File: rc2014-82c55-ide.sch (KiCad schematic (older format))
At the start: 13 parts, among them J1 CONN_02X06, J2 IDE connector, P1 RC2014 BUS, U1 82C55A_PLCC, U2 74HCT688, U3 74HCT04

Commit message: WIP
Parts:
- removed R2: 10K, Resistors_THT:R_Axial_DIN0207_L6.3mm_D2.5mm_P7.62mm_Horizontal, symbol R
- added J3: IDE connector, Pin_Headers:Pin_Header_Straight_2x22_Pitch2.00mm, symbol CONN_02X22
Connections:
- net labels added: RESET
- net labels removed: /INT0
- wire segments 166 -> 209
- no-connect marks 24 -> 30
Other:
- moved on the sheet: D1, J2, R1, U3B

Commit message: Relayout
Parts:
- removed J1: CONN_02X06, Pin_Headers:Pin_Header_Straight_2x06_Pitch2.54mm, symbol CONN_02X06
- added J1: CONN_02X13, Pin_Headers:Pin_Header_Straight_2x13_Pitch2.54mm, symbol CONN_02X13
- added SW1: SW_DIP_x06, Buttons_Switches_THT:SW_DIP_x6_W7.62mm_Slide, symbol SW_DIP_x06
- C1, C2, C3: footprint Capacitors_THT:C_Disc_D3.8mm_W2.6mm_P2.50mm -> Capacitors_THT:C_Disc_D3.0mm_W2.0mm_P2.50mm
- J2: footprint Pin_Headers:Pin_Header_Angled_2x20_Pitch2.54mm -> Pin_Headers:Pin_Header_Straight_2x20_Pitch2.54mm
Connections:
- net labels added: PC2, PC4, PC6
- net labels removed: INTRQ
- wire segments 209 -> 240
- no-connect marks 30 -> 32
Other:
- note removed: "TODO: INTRQ from drive?\n\nWiring this to the Z80s interrupt pin will cause issues when operating the Z80 in interrupt Mode 2. \nHave left it disconnected for the time being."
- moved on the sheet: J3, U3A, U3C, U3D, U3E, U3F

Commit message: WIP
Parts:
- removed J1: CONN_02X13, Pin_Headers:Pin_Header_Straight_2x13_Pitch2.54mm, symbol CONN_02X13
- added J1: CONN_01X02, Connectors:PINHEAD1-2, symbol CONN_01X02
- added J5: CONN_01X03, Pin_Headers:Pin_Header_Straight_1x03_Pitch2.54mm, symbol CONN_01X03
- D1: footprint LEDs:LED_D3.0mm_Horizontal_O3.81mm_Z6.0mm -> LEDs:LED_D1.8mm_W3.3mm_H2.4mm
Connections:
- net labels added: EXT_VCC, IDE_VCC
- wire segments 240 -> 219
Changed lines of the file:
@@
 F 0 "D1" H 6150 2300 50  0000 C CNN
 F 1 "LED" H 6150 2100 50  0000 C CNN
-F 2 "LEDs:LED_D3.0mm_Horizontal_O3.81mm_Z6.0mm" H 6150 2200 50  0001 C CNN
+F 2 "LEDs:LED_D1.8mm_W3.3mm_H2.4mm" H 6150 2200 50  0001 C CNN
 F 3 "" H 6150 2200 50  0001 C CNN
 	1    6150 2200
@@
 Text Label 10450 3600 0    60   ~ 0
 IDE-GND
-$Comp
-L VCC #PWR012
-U 1 1 59B846DB
-P 10850 3500
-F 0 "#PWR012" H 10850 3350 50  0001 C CNN
-F 1 "VCC" H 10850 3650 50  0000 C CNN
-F 2 "" H 10850 3500 50  0001 C CNN
-F 3 "" H 10850 3500 50  0001 C CNN
-	1    10850 3500
-	0    1    1    0
-$EndComp
-$Comp
-L VCC #PWR013
-U 1 1 59B84713
-P 9350 3500
-F 0 "#PWR013" H 9350 3350 50  0001 C CNN
-F 1 "VCC" H 9350 3650 50  0000 C CNN
-F 2 "" H 9350 3500 50  0001 C CNN
-F 3 "" H 9350 3500 50  0001 C CNN
-	1    9350 3500
-	0    -1   -1   0
-$EndComp
 NoConn ~ 9350 3000
 NoConn ~ 7650 3000
@@
 Wire Wire Line
 	6500 5650 7000 5650
-$Comp
-L CONN_02X13 J1
-U 1 1 59C02D49
-P 2950 4650
-F 0 "J1" H 2950 5350 50  0000 C CNN
-F 1 "CONN_02X13" V 2950 4650 50  0000 C CNN
-F 2 "Pin_Headers:Pin_Header_Straight_2x13_Pitch2.54mm" H 2950 3500 50  0001 C CNN
-F 3 "" H 2950 3500 50  0001 C CNN
-	1    2950 4650
-	1    0    0    -1
-$EndComp
-Wire Wire Line
-	2700 4050 2350 4050
-Wire Wire Line
-	2700 4150 2350 4150
-Wire Wire Line
-	2700 4250 2350 4250
-Wire Wire Line
-	2700 4350 2350 4350
-Wire Wire Line
-	2700 4450 2350 4450
-Wire Wire Line
-	2700 4550 2350 4550
-Wire Wire Line
-	2700 4650 2350 4650
-Wire Wire Line
-	2700 4750 2350 4750
-Wire Wire Line
-	2700 4850 2350 4850
-Wire Wire Line
-	2700 4950 2350 4950
-Wire Wire Line
-	2700 5050 2350 5050
-Wire Wire Line
-	2700 5150 2350 5150
-Wire Wire Line
-	2700 5250 2350 5250
-Wire Wire Line
-	3550 4050 3200 4050
-Wire Wire Line
-	3200 4150 3550 4150
-Wire Wire Line
-	3200 4250 3550 4250
-Wire Wire Line
-	3200 4350 3550 4350
-Wire Wire Line
-	3200 4450 3550 4450
-Wire Wire Line
-	3200 4550 3550 4550
-Wire Wire Line
-	3200 4650 3550 4650
-Wire Wire Line
-	3200 4750 3550 4750
-Wire Wire Line
-	3200 4850 3550 4850
-Wire Wire Line
-	3200 4950 3550 4950
-Wire Wire Line
-	3200 5050 3550 5050
-Wire Wire Line
-	3200 5150 3550 5150
-Wire Wire Line
-	3200 5250 3550 5250
-Text Label 2400 4050 0    60   ~ 0
-PC0
-Text Label 2400 4150 0    60   ~ 0
-PC1
-Text Label 2400 4250 0    60   ~ 0
-PC2
-Text Label 2400 4350 0    60   ~ 0
-PC3
-Text Label 2400 4450 0    60   ~ 0
-PC4
-Text Label 2400 4550 0    60   ~ 0
-PC5
-Text Label 2400 4650 0    60   ~ 0
-PC6
-Text Label 2400 4750 0    60   ~ 0
-PC7
-Text Label 2400 4850 0    60   ~ 0
-PB7
-Text Label 2400 4950 0    60   ~ 0
-PB6
-Text Label 2400 5050 0    60   ~ 0
-PB5
-Text Label 2400 5150 0    60   ~ 0
-PB4
-Text Label 3350 4050 0    60   ~ 0
-PA0
-Text Label 3350 4150 0    60   ~ 0
-PA1
-Text Label 3350 4250 0    60   ~ 0
-PA2
-Text Label 3350 4350 0    60   ~ 0
-PA3
-Text Label 3350 4450 0    60   ~ 0
-PA4
-Text Label 3350 4550 0    60   ~ 0
-PA5
-Text Label 3350 4650 0    60   ~ 0
-PA6
-Text Label 3350 4750 0    60   ~ 0
-PA7
-Text Label 3350 4850 0    60   ~ 0
-PB0
-Text Label 3350 4950 0    60   ~ 0
-PB1
-Text Label 3350 5050 0    60   ~ 0
-PB2
-Text Label 3350 5150 0    60   ~ 0
-PB3
-$Comp
-L GND #PWR014
-U 1 1 59C031E2
-P 3550 5250
-F 0 "#PWR014" H 3550 5000 50  0001 C CNN
-F 1 "GND" H 3550 5100 50  0000 C CNN
-F 2 "" H 3550 5250 50  0001 C CNN
-F 3 "" H 3550 5250 50  0001 C CNN
-	1    3550 5250
-	1    0    0    -1
-$EndComp
 Text Label 9150 6250 0    60   ~ 0
 PC7
@@
 PC3
 $Comp
-L VCC #PWR015
-U 1 1 59C0A089
-P 2350 5250
-F 0 "#PWR015" H 2350 5100 50  0001 C CNN
-F 1 "VCC" H 2350 5400 50  0000 C CNN
-F 2 "" H 2350 5250 50  0001 C CNN
-F 3 "" H 2350 5250 50  0001 C CNN
-	1    2350 5250
-	0    -1   -1   0
-$EndComp
-$Comp
 L SW_DIP_x06 SW1
 U 1 1 59C0ABDD
@@
 Text Label 7100 5150 0    60   ~ 0
 DA2
+$Comp
+L CONN_01X03 J5
+U 1 1 59C1C7A5
+P 8250 5000
+F 0 "J5" H 8250 5200 50  0000 C CNN
+F 1 "CONN_01X03" V 8350 5000 50  0000 C CNN
+F 2 "Pin_Headers:Pin_Header_Straight_1x03_Pitch2.54mm" H 8250 5000 50  0001 C CNN
+F 3 "" H 8250 5000 50  0001 C CNN
+	1    8250 5000
+	1    0    0    -1
+$EndComp
+Wire Wire Line
+	8050 4900 7800 4900
+Wire Wire Line
+	8050 5000 7800 5000
+Wire Wire Line
+	8050 5100 7800 5100
+Text Label 7800 5000 0    60   ~ 0
+IDE_VCC
+Text Label 7800 5100 0    60   ~ 0
+EXT_VCC
+$Comp
+L VCC #PWR012
+U 1 1 59C1C979
+P 7800 4900
+F 0 "#PWR012" H 7800 4750 50  0001 C CNN
+F 1 "VCC" H 7800 5050 50  0000 C CNN
+F 2 "" H 7800 4900 50  0001 C CNN
+F 3 "" H 7800 4900 50  0001 C CNN
+	1    7800 4900
+	0    -1   -1   0
+$EndComp
+$Comp
+L CONN_01X02 J1
+U 1 1 59C1C9D2
+P 8200 6000
+F 0 "J1" H 8200 6150 50  0000 C CNN
+F 1 "CONN_01X02" V 8300 6000 50  0000 C CNN
+F 2 "Connectors:PINHEAD1-2" H 8200 6000 50  0001 C CNN
+F 3 "" H 8200 6000 50  0001 C CNN
+	1    8200 6000
+	1    0    0    -1
+$EndComp
+Wire Wire Line
+	8000 5950 7750 5950
+Wire Wire Line
+	8000 6050 7750 6050
+Text Label 7750 5950 0    60   ~ 0
+EXT_VCC
+Text Label 9350 3500 0    60   ~ 0
+IDE_VCC
+Text Label 10500 3500 0    60   ~ 0
+IDE_VCC
+$Comp
+L GND #PWR013
+U 1 1 59C1D145
+P 7750 6050
+F 0 "#PWR013" H 7750 5800 50  0001 C CNN
+F 1 "GND" H 7750 5900 50  0000 C CNN
+F 2 "" H 7750 6050 50  0001 C CNN
+F 3 "" H 7750 6050 50  0001 C CNN
+	1    7750 6050
+	1    0    0    -1
+$EndComp
 $EndSCHEMATC

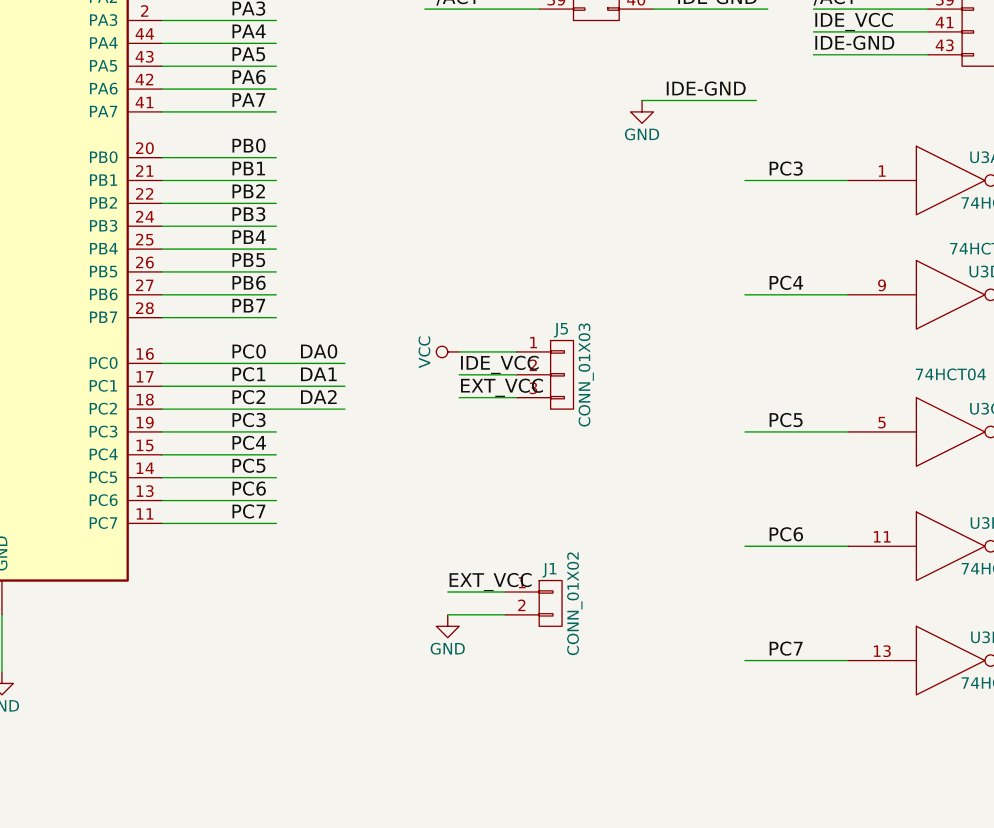
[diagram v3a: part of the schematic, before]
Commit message: Add jumpers
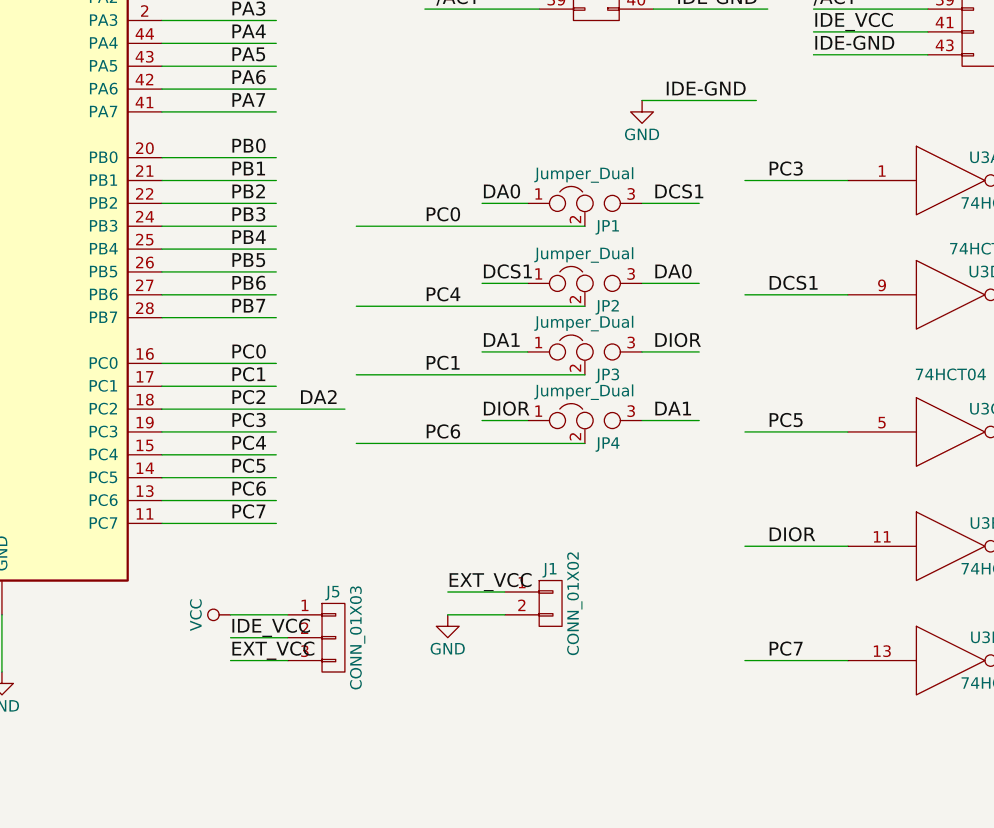
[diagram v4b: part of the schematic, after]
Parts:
- added JP1, JP2, JP3, JP4: Jumper_Dual, symbol Jumper_Dual
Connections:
- net labels added: DCS1, DIOR
- wire segments 219 -> 232
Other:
- moved on the sheet: J5
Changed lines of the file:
@@
 5V
 $Comp
-L VCC #PWR01
+L VCC #PWR2
 U 1 1 5898D2A5
 P 1350 3500
-F 0 "#PWR01" H 1350 3350 50  0001 C CNN
+F 0 "#PWR2" H 1350 3350 50  0001 C CNN
 F 1 "VCC" H 1600 3500 50  0000 C CNN
 F 2 "" H 1350 3500 50  0000 C CNN
@@
 $EndComp
 $Comp
-L PWR_FLAG #FLG02
+L PWR_FLAG #FLG2
 U 1 1 58E0E873
 P 1550 3400
-F 0 "#FLG02" H 1550 3475 50  0001 C CNN
+F 0 "#FLG2" H 1550 3475 50  0001 C CNN
 F 1 "PWR_FLAG" H 1900 3400 50  0000 C CNN
 F 2 "" H 1550 3400 50  0001 C CNN
@@
 $EndComp
 $Comp
-L PWR_FLAG #FLG03
+L PWR_FLAG #FLG1
 U 1 1 58E0EDBF
 P 1450 3500
-F 0 "#FLG03" H 1450 3575 50  0001 C CNN
+F 0 "#FLG1" H 1450 3575 50  0001 C CNN
 F 1 "PWR_FLAG" H 1900 3500 50  0000 C CNN
 F 2 "" H 1450 3500 50  0001 C CNN
@@
 A1
 $Comp
-L VCC #PWR04
+L VCC #PWR6
 U 1 1 59B6DE88
 P 5800 2700
-F 0 "#PWR04" H 5800 2550 50  0001 C CNN
+F 0 "#PWR6" H 5800 2550 50  0001 C CNN
 F 1 "VCC" H 5800 2850 50  0000 C CNN
 F 2 "" H 5800 2700 50  0001 C CNN
@@
 $EndComp
 $Comp
-L GND #PWR05
+L GND #PWR7
 U 1 1 59B6DEAC
 P 5800 6300
-F 0 "#PWR05" H 5800 6050 50  0001 C CNN
+F 0 "#PWR7" H 5800 6050 50  0001 C CNN
 F 1 "GND" H 5800 6150 50  0000 C CNN
 F 2 "" H 5800 6300 50  0001 C CNN
@@
 $EndComp
 $Comp
-L VCC #PWR06
+L VCC #PWR8
 U 1 1 59B6FC74
 P 6450 2200
-F 0 "#PWR06" H 6450 2050 50  0001 C CNN
+F 0 "#PWR8" H 6450 2050 50  0001 C CNN
 F 1 "VCC" H 6450 2350 50  0000 C CNN
 F 2 "" H 6450 2200 50  0001 C CNN
@@
 $EndComp
 $Comp
-L GND #PWR07
+L GND #PWR5
 U 1 1 59B6FD29
 P 3350 3250
-F 0 "#PWR07" H 3350 3000 50  0001 C CNN
+F 0 "#PWR5" H 3350 3000 50  0001 C CNN
 F 1 "GND" H 3350 3100 50  0000 C CNN
 F 2 "" H 3350 3250 50  0001 C CNN
@@
 $EndComp
 $Comp
-L VCC #PWR08
+L VCC #PWR3
 U 1 1 59B6FD5B
 P 1900 2650
-F 0 "#PWR08" H 1900 2500 50  0001 C CNN
+F 0 "#PWR3" H 1900 2500 50  0001 C CNN
 F 1 "VCC" H 1900 2800 50  0000 C CNN
 F 2 "" H 1900 2650 50  0001 C CNN
@@
 	6500 4750 7000 4750
 Wire Wire Line
-	6500 4950 7300 4950
-Wire Wire Line
-	6500 5050 7300 5050
+	6500 4950 7000 4950
+Wire Wire Line
+	6500 5050 7000 5050
 Wire Wire Line
 	6500 5150 7300 5150
@@
 	8600 3800 9100 3800
 $Comp
-L GND #PWR09
+L GND #PWR11
 U 1 1 59B735A8
 P 8600 3800
-F 0 "#PWR09" H 8600 3550 50  0001 C CNN
+F 0 "#PWR11" H 8600 3550 50  0001 C CNN
 F 1 "GND" H 8600 3650 50  0000 C CNN
 F 2 "" H 8600 3800 50  0001 C CNN
@@
 Connection ~ 2000 6600
 $Comp
-L GND #PWR010
+L GND #PWR4
 U 1 1 59B7399E
 P 2750 6700
-F 0 "#PWR010" H 2750 6450 50  0001 C CNN
+F 0 "#PWR4" H 2750 6450 50  0001 C CNN
 F 1 "GND" H 2750 6550 50  0000 C CNN
 F 2 "" H 2750 6700 50  0001 C CNN
@@
 $EndComp
 $Comp
-L VCC #PWR011
+L VCC #PWR1
 U 1 1 59B739D6
 P 1250 6200
-F 0 "#PWR011" H 1250 6050 50  0001 C CNN
+F 0 "#PWR1" H 1250 6050 50  0001 C CNN
 F 1 "VCC" H 1250 6350 50  0000 C CNN
 F 2 "" H 1250 6200 50  0001 C CNN
@@
 Text Label 9150 5250 0    60   ~ 0
 PC5
-Text Label 9150 5750 0    60   ~ 0
-PC6
-Text Label 9150 4650 0    60   ~ 0
-PC4
 Text Label 9150 4150 0    60   ~ 0
 PC3
@@
 	1    0    0    -1
 $EndComp
-Text Label 7100 4950 0    60   ~ 0
-DA0
-Text Label 7100 5050 0    60   ~ 0
-DA1
 Text Label 7100 5150 0    60   ~ 0
 DA2
@@
 L CONN_01X03 J5
 U 1 1 59C1C7A5
-P 8250 5000
-F 0 "J5" H 8250 5200 50  0000 C CNN
-F 1 "CONN_01X03" V 8350 5000 50  0000 C CNN
-F 2 "Pin_Headers:Pin_Header_Straight_1x03_Pitch2.54mm" H 8250 5000 50  0001 C CNN
-F 3 "" H 8250 5000 50  0001 C CNN
-	1    8250 5000
-	1    0    0    -1
-$EndComp
-Wire Wire Line
-	8050 4900 7800 4900
-Wire Wire Line
-	8050 5000 7800 5000
-Wire Wire Line
-	8050 5100 7800 5100
-Text Label 7800 5000 0    60   ~ 0
+P 7250 6150
+F 0 "J5" H 7250 6350 50  0000 C CNN
+F 1 "CONN_01X03" V 7350 6150 50  0000 C CNN
+F 2 "Pin_Headers:Pin_Header_Straight_1x03_Pitch2.54mm" H 7250 6150 50  0001 C CNN
+F 3 "" H 7250 6150 50  0001 C CNN
+	1    7250 6150
+	1    0    0    -1
+$EndComp
+Wire Wire Line
+	7050 6050 6800 6050
+Wire Wire Line
+	7050 6150 6800 6150
+Wire Wire Line
+	7050 6250 6800 6250
+Text Label 6800 6150 0    60   ~ 0
 IDE_VCC
-Text Label 7800 5100 0    60   ~ 0
+Text Label 6800 6250 0    60   ~ 0
 EXT_VCC
 $Comp
-L VCC #PWR012
+L VCC #PWR9
 U 1 1 59C1C979
-P 7800 4900
-F 0 "#PWR012" H 7800 4750 50  0001 C CNN
-F 1 "VCC" H 7800 5050 50  0000 C CNN
-F 2 "" H 7800 4900 50  0001 C CNN
-F 3 "" H 7800 4900 50  0001 C CNN
-	1    7800 4900
+P 6800 6050
+F 0 "#PWR9" H 6800 5900 50  0001 C CNN
+F 1 "VCC" H 6800 6200 50  0000 C CNN
+F 2 "" H 6800 6050 50  0001 C CNN
+F 3 "" H 6800 6050 50  0001 C CNN
+	1    6800 6050
 	0    -1   -1   0
 $EndComp
@@
 IDE_VCC
 $Comp
-L GND #PWR013
+L GND #PWR10
 U 1 1 59C1D145
 P 7750 6050
-F 0 "#PWR013" H 7750 5800 50  0001 C CNN
+F 0 "#PWR10" H 7750 5800 50  0001 C CNN
 F 1 "GND" H 7750 5900 50  0000 C CNN
 F 2 "" H 7750 6050 50  0001 C CNN
@@
 	1    0    0    -1
 $EndComp
+Wire Wire Line
+	7350 5300 8350 5300
+Wire Wire Line
+	7350 5000 8350 5000
+Text Label 9150 4650 0    60   ~ 0
+DCS1
+Text Label 9150 5750 0    60   ~ 0
+DIOR
+Text Label 7650 4350 0    60   ~ 0
+PC0
+Text Label 7650 5000 0    60   ~ 0
+PC1
+Wire Wire Line
+	7350 4350 8350 4350
+Wire Wire Line
+	7350 4700 8350 4700
+Text Label 7900 4250 0    60   ~ 0
+DA0
+Text Label 7900 4900 0    60   ~ 0
+DA1
+Text Label 7650 4700 0    60   ~ 0
+PC4
+Text Label 7900 4600 0    60   ~ 0
+DCS1
+Text Label 7650 5300 0    60   ~ 0
+PC6
+Text Label 7900 5200 0    60   ~ 0
+DIOR
+Wire Wire Line
+	8550 5350 8550 5350
+$Comp
+L Jumper_Dual JP1
+U 1 1 59C55EB0
+P 8350 4250
+F 0 "JP1" H 8400 4150 50  0000 L CNN
+F 1 "Jumper_Dual" H 8350 4350 50  0000 C BNN
+F 2 "" H 8350 4250 50  0001 C CNN
+F 3 "" H 8350 4250 50  0001 C CNN
+	1    8350 4250
+	1    0    0    -1
+$EndComp
+$Comp
+L Jumper_Dual JP2
+U 1 1 59C55FBB
+P 8350 4600
+F 0 "JP2" H 8400 4500 50  0000 L CNN
+F 1 "Jumper_Dual" H 8350 4700 50  0000 C BNN
+F 2 "" H 8350 4600 50  0001 C CNN
+F 3 "" H 8350 4600 50  0001 C CNN
+	1    8350 4600
+	1    0    0    -1
+$EndComp
+$Comp
+L Jumper_Dual JP3
+U 1 1 59C56029
+P 8350 4900
+F 0 "JP3" H 8400 4800 50  0000 L CNN
+F 1 "Jumper_Dual" H 8350 5000 50  0000 C BNN
+F 2 "" H 8350 4900 50  0001 C CNN
+F 3 "" H 8350 4900 50  0001 C CNN
+	1    8350 4900
+	1    0    0    -1
+$EndComp
+$Comp
+L Jumper_Dual JP4
+U 1 1 59C561E0
+P 8350 5200
+F 0 "JP4" H 8400 5100 50  0000 L CNN
+F 1 "Jumper_Dual" H 8350 5300 50  0000 C BNN
+F 2 "" H 8350 5200 50  0001 C CNN
+F 3 "" H 8350 5200 50  0001 C CNN
+	1    8350 5200
+	1    0    0    -1
+$EndComp
+Wire Wire Line
+	8100 4250 7900 4250
+Wire Wire Line
+	8100 4600 7900 4600
+Wire Wire Line
+	8600 4250 8850 4250
+Wire Wire Line
+	8600 4600 8850 4600
+Wire Wire Line
+	8100 4900 7900 4900
+Wire Wire Line
+	8100 5200 7900 5200
+Wire Wire Line
+	8600 4900 8850 4900
+Wire Wire Line
+	8600 5200 8850 5200
+Text Label 8650 4250 0    60   ~ 0
+DCS1
+Text Label 8650 4600 0    60   ~ 0
+DA0
+Text Label 8650 5200 0    60   ~ 0
+DA1
+Text Label 8650 4900 0    60   ~ 0
+DIOR
 $EndSCHEMATC

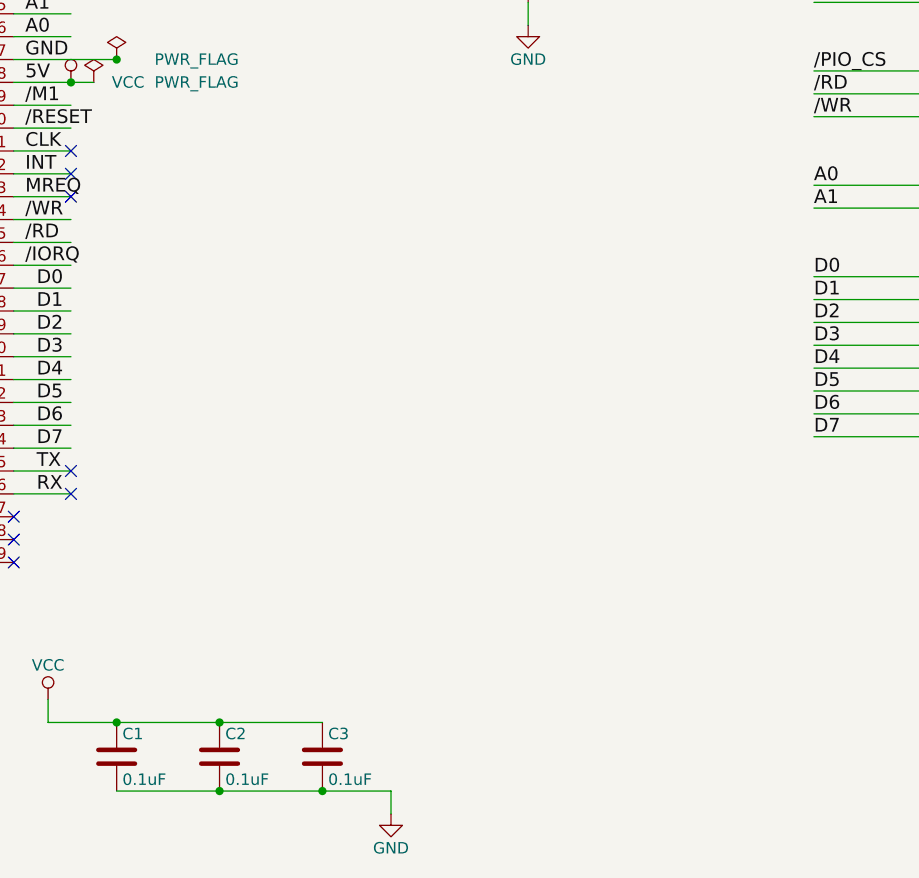
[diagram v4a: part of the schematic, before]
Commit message: add rtc
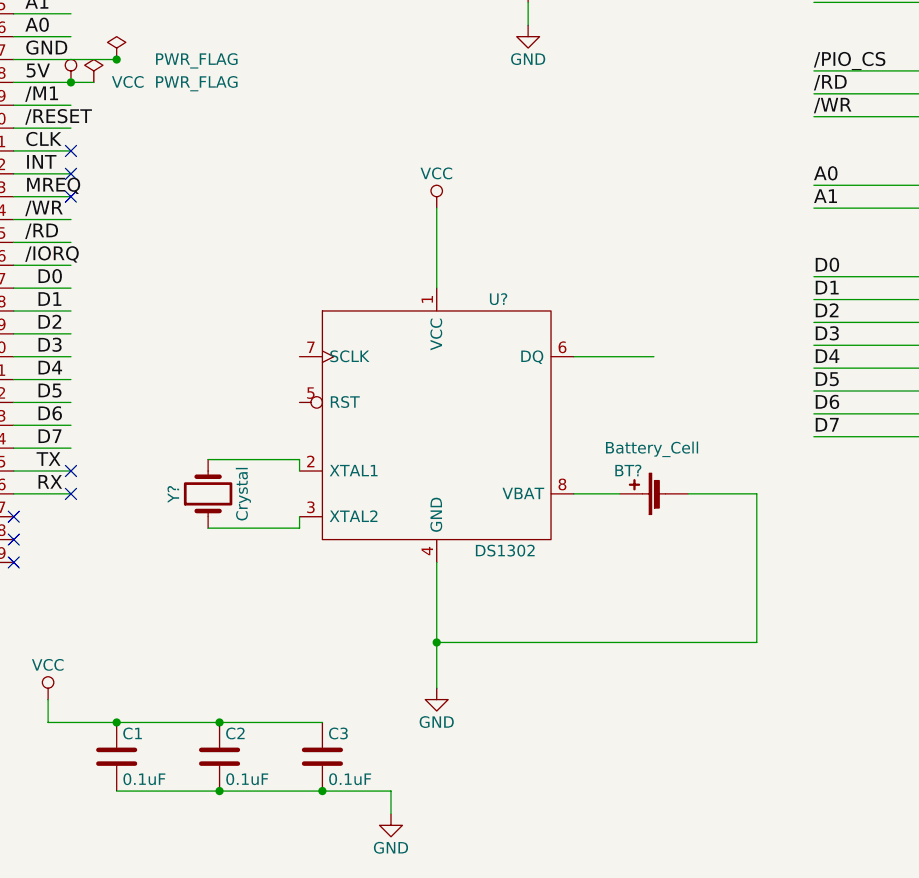
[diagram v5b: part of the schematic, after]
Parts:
- added BT?: Battery_Cell, symbol Battery_Cell
- added U?: DS1302, symbol DS1302
- added Y?: Crystal, symbol Crystal
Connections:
- wire segments 232 -> 243
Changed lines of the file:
@@
 LIBS:jumper_dual
 LIBS:switches
+LIBS:maxim
 LIBS:rc2014-82c55-ide-cache
 EELAYER 25 0
@@
 Text Label 8650 4900 0    60   ~ 0
 DIOR
+$Comp
+L DS1302 U?
+U 1 1 59C5373F
+P 2950 5000
+F 0 "U?" H 3220 5550 50  0000 C CNN
+F 1 "DS1302" H 3250 4450 50  0000 C CNN
+F 2 "" H 2950 5000 50  0000 C CNN
+F 3 "" H 2950 5000 50  0000 C CNN
+	1    2950 5000
+	1    0    0    -1
+$EndComp
+$Comp
+L Crystal Y?
+U 1 1 59C537A8
+P 1950 5300
+F 0 "Y?" H 1950 5450 50  0000 C CNN
+F 1 "Crystal" H 1950 5150 50  0000 C CNN
+F 2 "" H 1950 5300 50  0000 C CNN
+F 3 "" H 1950 5300 50  0000 C CNN
+	1    1950 5300
+	0    -1   -1   0
+$EndComp
+$Comp
+L Battery_Cell BT?
+U 1 1 59C53806
+P 3950 5300
+F 0 "BT?" V 4050 5400 50  0000 L CNN
+F 1 "Battery_Cell" V 4150 5150 50  0000 L CNN
+F 2 "" V 3950 5360 50  0000 C CNN
+F 3 "" V 3950 5360 50  0000 C CNN
+	1    3950 5300
+	0    -1   -1   0
+$EndComp
+Wire Wire Line
+	2950 4050 2950 4400
+Wire Wire Line
+	2950 5600 2950 6150
+Wire Wire Line
+	3550 4700 3900 4700
+Wire Wire Line
+	3750 5300 3550 5300
+Wire Wire Line
+	4050 5300 4350 5300
+Wire Wire Line
+	4350 5300 4350 5950
+Wire Wire Line
+	4350 5950 2950 5950
+Connection ~ 2950 5950
+$Comp
+L GND #PWR?
+U 1 1 59C54569
+P 2950 6150
+F 0 "#PWR?" H 2950 5900 50  0001 C CNN
+F 1 "GND" H 2950 6000 50  0000 C CNN
+F 2 "" H 2950 6150 50  0000 C CNN
+F 3 "" H 2950 6150 50  0000 C CNN
+	1    2950 6150
+	1    0    0    -1
+$EndComp
+$Comp
+L VCC #PWR?
+U 1 1 59C545CE
+P 2950 4050
+F 0 "#PWR?" H 2950 3900 50  0001 C CNN
+F 1 "VCC" H 2950 4200 50  0000 C CNN
+F 2 "" H 2950 4050 50  0000 C CNN
+F 3 "" H 2950 4050 50  0000 C CNN
+	1    2950 4050
+	1    0    0    -1
+$EndComp
+Wire Wire Line
+	1950 5450 2350 5450
+Wire Wire Line
+	2350 5450 2350 5400
+Wire Wire Line
+	2350 5200 2350 5150
+Wire Wire Line
+	2350 5150 1950 5150
 $EndSCHEMATC
